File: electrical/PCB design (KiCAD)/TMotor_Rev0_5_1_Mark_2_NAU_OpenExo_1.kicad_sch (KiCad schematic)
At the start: 17 parts, among them U5 TXU0104PWR, U6 TXU0304-Q1, U7 DEV-16771

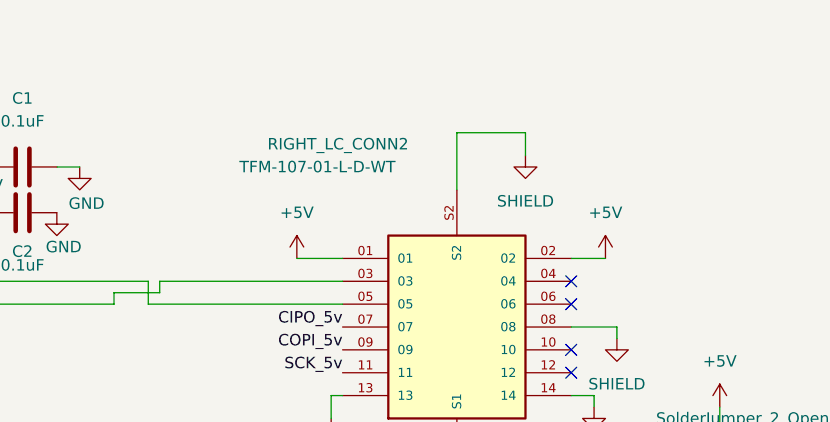
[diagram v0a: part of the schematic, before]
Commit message: fixed singleLeg python scripts
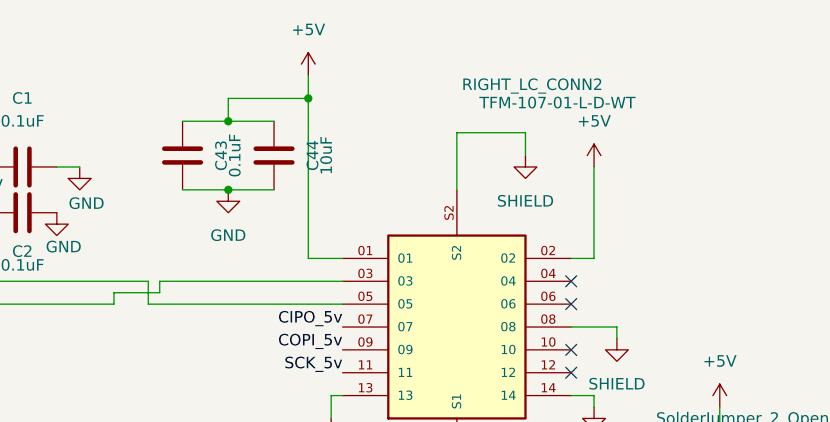
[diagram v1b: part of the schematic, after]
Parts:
- added C43: 0.1uF, Capacitor_SMD:C_0805_2012Metric_Pad1.18x1.45mm_HandSolder, symbol Device:C
- added C44: 10uF, Capacitor_SMD:C_0805_2012Metric_Pad1.18x1.45mm_HandSolder, symbol Device:C
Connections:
- net +5V: now also C43.2, C44.2
- net GND: now also C43.1, C44.1

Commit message: code refactoring for clarity
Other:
- note added: "Is there going to be a problem if both Teensy and Nano power the 3.3V line simultaneously???"
- note removed: "ADD A SOLDER JUMPER HERE?"
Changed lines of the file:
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@@
 	(generator_version "10.0")
 	(paper "A4")
-	(text "ADD A SOLDER JUMPER HERE?"
+	(arc
+		(start 48.26 162.56)
+		(mid 55.3539 158.1337)
+		(end 63.5 160.02)
+		(stroke
+			(width 0)
+			(type default)
+		)
+		(fill
+			(type none)
+		)
+	)
+	(text "Is there going to be a problem \nif both Teensy and Nano power the 3.3V line \nsimultaneously???"
 		(exclude_from_sim no)
-		(at 39.37 160.02 0)
+		(at 34.544 166.878 0)
 		(effects
 			(font
@@
 	)
 	(no_connect
+		(at 64.77 161.29)
+	)
+	(no_connect
 		(at 223.52 127)
 	)
@@
 	)
 	(no_connect
-		(at 64.77 161.29)
-	)
-	(no_connect
